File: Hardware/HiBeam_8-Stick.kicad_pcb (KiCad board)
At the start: 2 copper layers, 56.5 x 14.6 mm, 20 parts, among them J1 CONN_041X04_NO_SILK, J2 CONN_041X04_NO_SILK, U1 APA102, U2 APA102, U3 APA102, U4 APA102, U5 APA102, U6 APA102, U7 APA102, U8 APA102

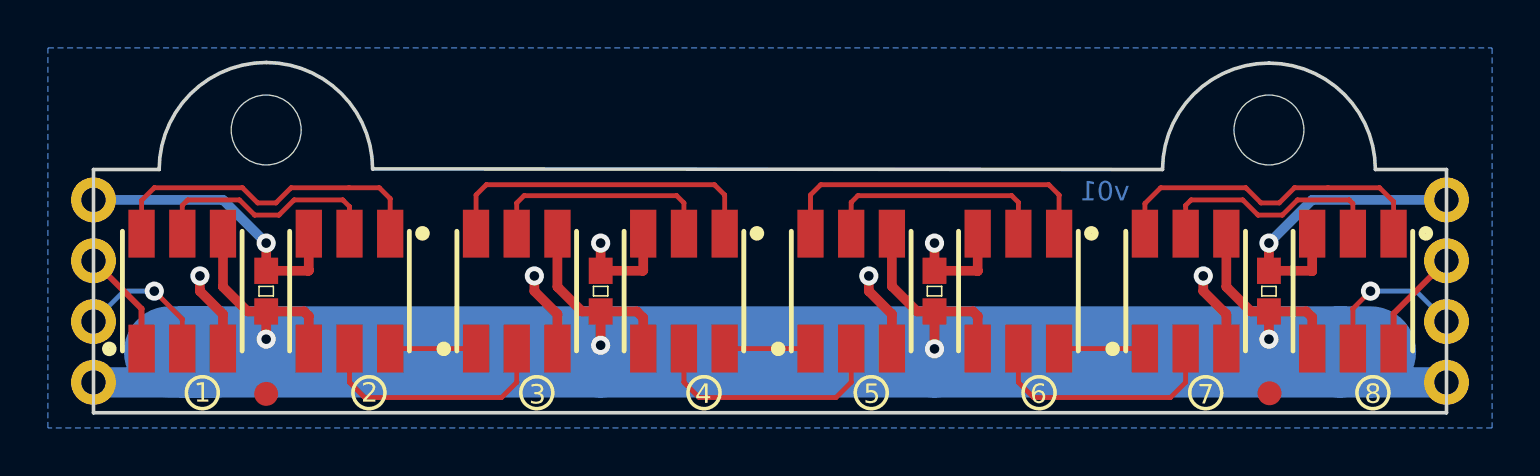
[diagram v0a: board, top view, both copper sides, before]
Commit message: Added solder jumpers on the output lines.
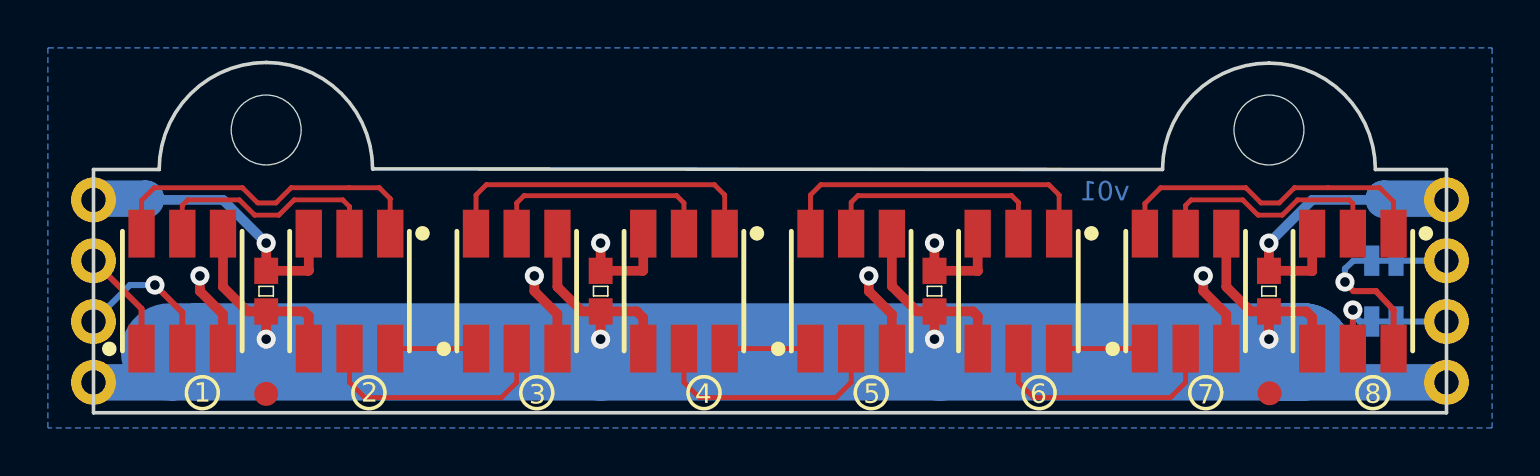
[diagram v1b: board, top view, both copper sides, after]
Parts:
- added JP1: JUMPER-SMT_2_NC_TRACE_SILK, Pete:SMT-JUMPER_2_NC_TRACE_SILK, B.Cu at (174.5, 104.1)
- added JP2: JUMPER-SMT_2_NC_TRACE_SILK, Pete:SMT-JUMPER_2_NC_TRACE_SILK, B.Cu at (174.5, 101.6)
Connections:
- U8 pad 5: /CO -> Net-(JP1-Pad1)
- U8 pad 6: /DO -> Net-(JP2-Pad1)
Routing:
- net Net-(JP2-Pad1): track 0.00 -> 5.96 mm, vias 0 -> 1
- net GND: track 47.9 -> 52.8 mm
- net /CO: track 6.41 -> 2.11 mm, vias 1 -> 0
- net +5V: track 101.7 -> 105.4 mm
- net Net-(JP1-Pad1): track 0.00 -> 2.68 mm, vias 0 -> 1
- net /DO: track 4.59 -> 2.11 mm
